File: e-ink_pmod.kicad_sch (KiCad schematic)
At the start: 22 parts, among them Q1 Q_NMOS_GSD, U1 23K640-I/SN, X1 52435-2471

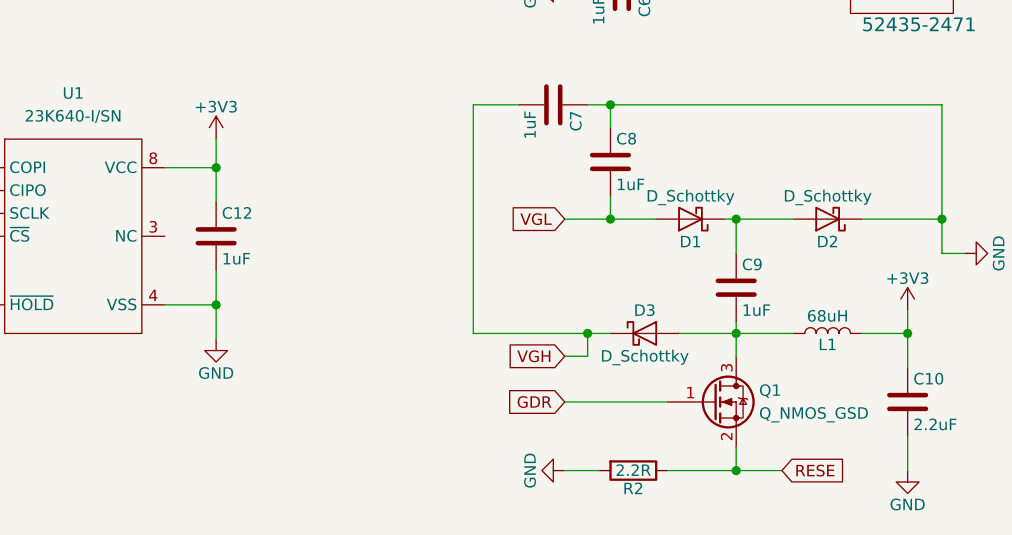
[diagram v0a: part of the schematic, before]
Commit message: Updated documentation
Also updated KiCad version for better compatibility with KiCanvas

Signed-off-by: Thomas Flummer <tf@flummer.net>
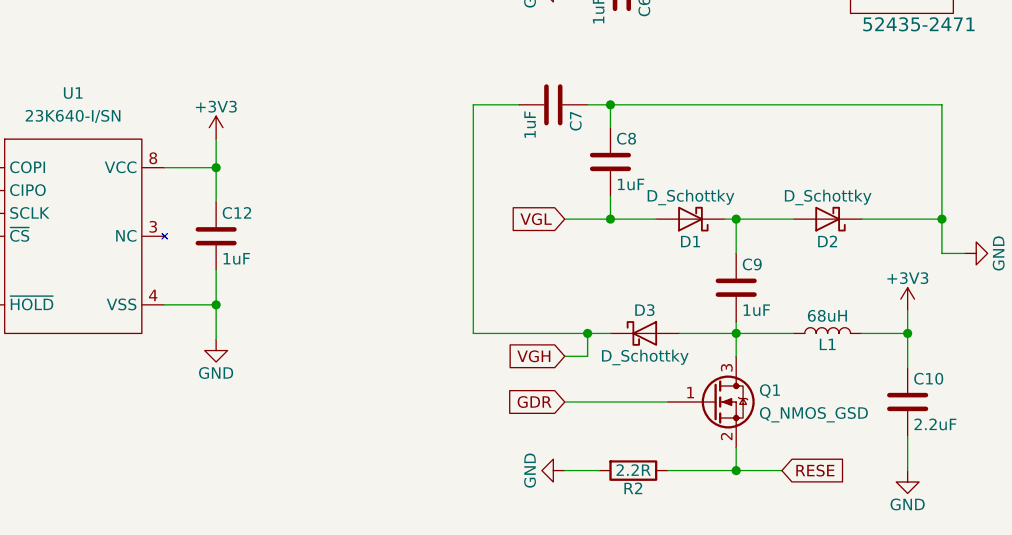
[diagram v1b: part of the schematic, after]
